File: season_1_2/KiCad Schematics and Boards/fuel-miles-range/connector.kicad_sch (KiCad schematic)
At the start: 1 part, among them J601 Conn_02x06_Top_Bottom

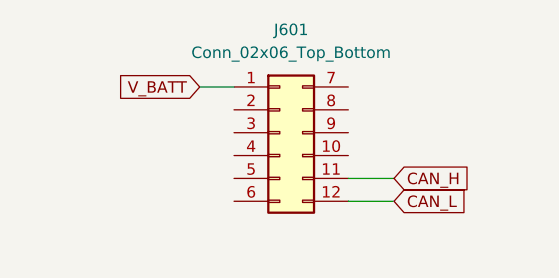
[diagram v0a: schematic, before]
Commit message: Added lots of electronic devices and routes
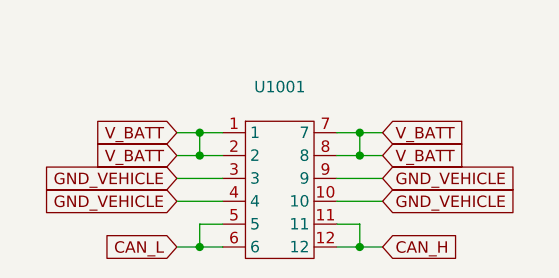
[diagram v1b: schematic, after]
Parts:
- removed J601: Conn_02x06_Top_Bottom, Connector_IDC:IDC-Header_2x06_P2.54mm_Vertical, symbol Connector_Generic:Conn_02x06_Top_Bottom
- added U1001: ~, Code99_Conn:TE-967646-1, symbol Code99_Conn:TE-967646-1
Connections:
- net CAN_H: now also U1001.11, U1001.12
- net CAN_L: now also U1001.5, U1001.6
- net V_BATT: now also U1001.1, U1001.2, U1001.7, U1001.8
- new net GND_VEHICLE: U1001.10, U1001.3, U1001.4, U1001.9

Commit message: Added 4 missing wires for LED BAR 3, added programming PINs for STM32
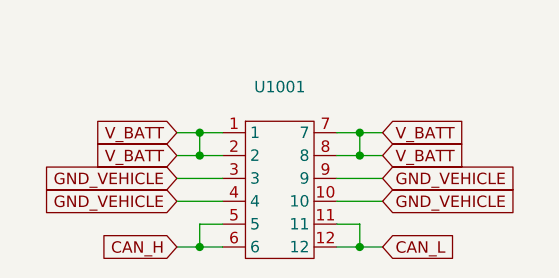
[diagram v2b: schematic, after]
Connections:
- net CAN_H: now also U1001.5, U1001.6; no longer U1001.11, U1001.12
- net CAN_L: now also U1001.11, U1001.12; no longer U1001.5, U1001.6
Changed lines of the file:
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@@
 		)
 	)
-	(global_label "CAN_H"
+	(global_label "CAN_L"
 		(shape input)
 		(at 161.29 105.41 0)
@@
 		)
 		(property "Intersheetrefs" "${INTERSHEET_REFS}"
-			(at 170.2624 105.41 0)
+			(at 169.96 105.41 0)
 			(effects
 				(font
@@
 		)
 	)
-	(global_label "CAN_L"
+	(global_label "CAN_H"
 		(shape input)
 		(at 138.43 105.41 180)
@@
 		)
 		(property "Intersheetrefs" "${INTERSHEET_REFS}"
-			(at 129.76 105.41 0)
+			(at 129.4576 105.41 0)
 			(effects
 				(font
